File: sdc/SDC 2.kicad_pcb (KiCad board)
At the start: 2 copper layers, 70 x 45 mm, 90 parts, among them J1 Conn_02x10_Odd_Even, K1 G2RL-2A, K2 G2RL-2A, K3 G2RL-2A, K4 G2RL-2A, Q1 2N7002, Q2 2N7002, Q3 2N7002, Q4 2N7002, Q5 2N7002, Q6 2N7002, U1 VOM618AT, U10 AP2204K-ADJ, U2 VOM618AT, U3 TLV2371DBV, U4 TLV2371DBV, U6 VOM618AT, U7 VOM618AT, U8 TLV2371DBV, U9 AP2204K-ADJ

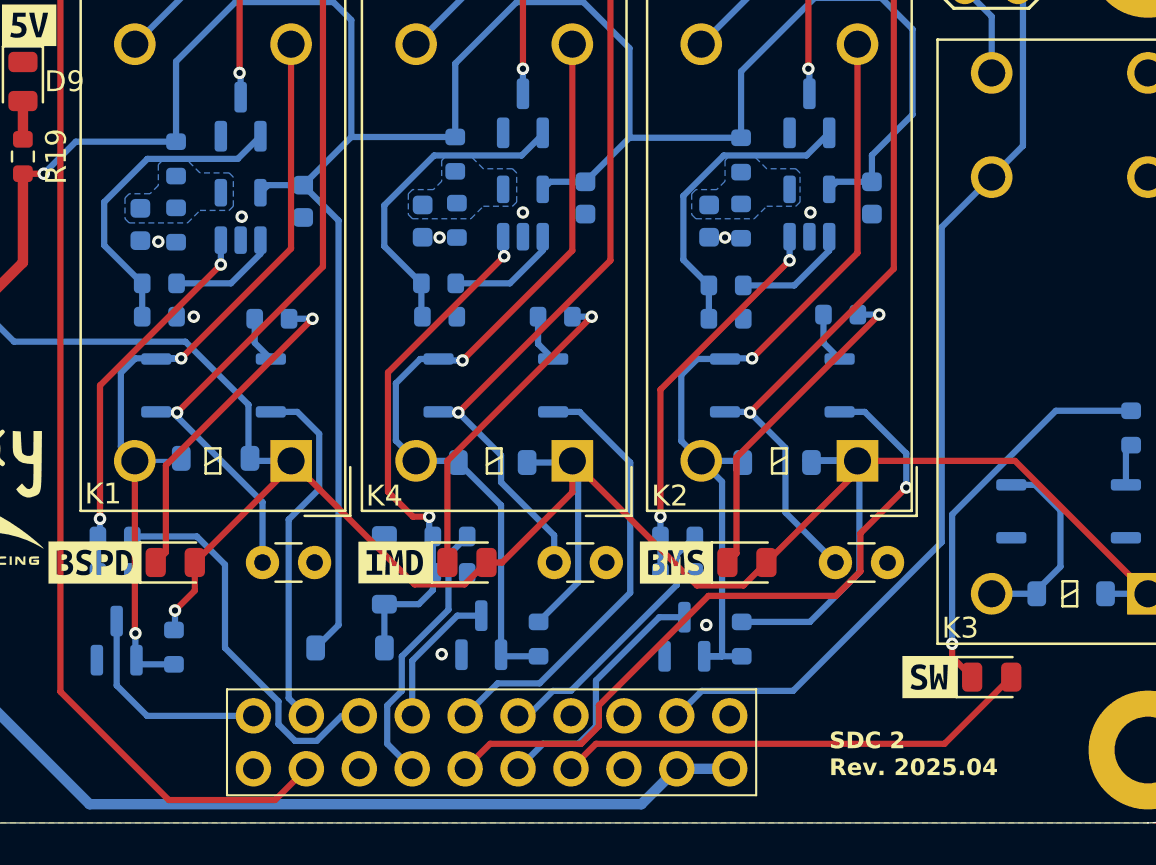
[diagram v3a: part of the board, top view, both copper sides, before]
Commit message: change comparator to AS331KTR-G1
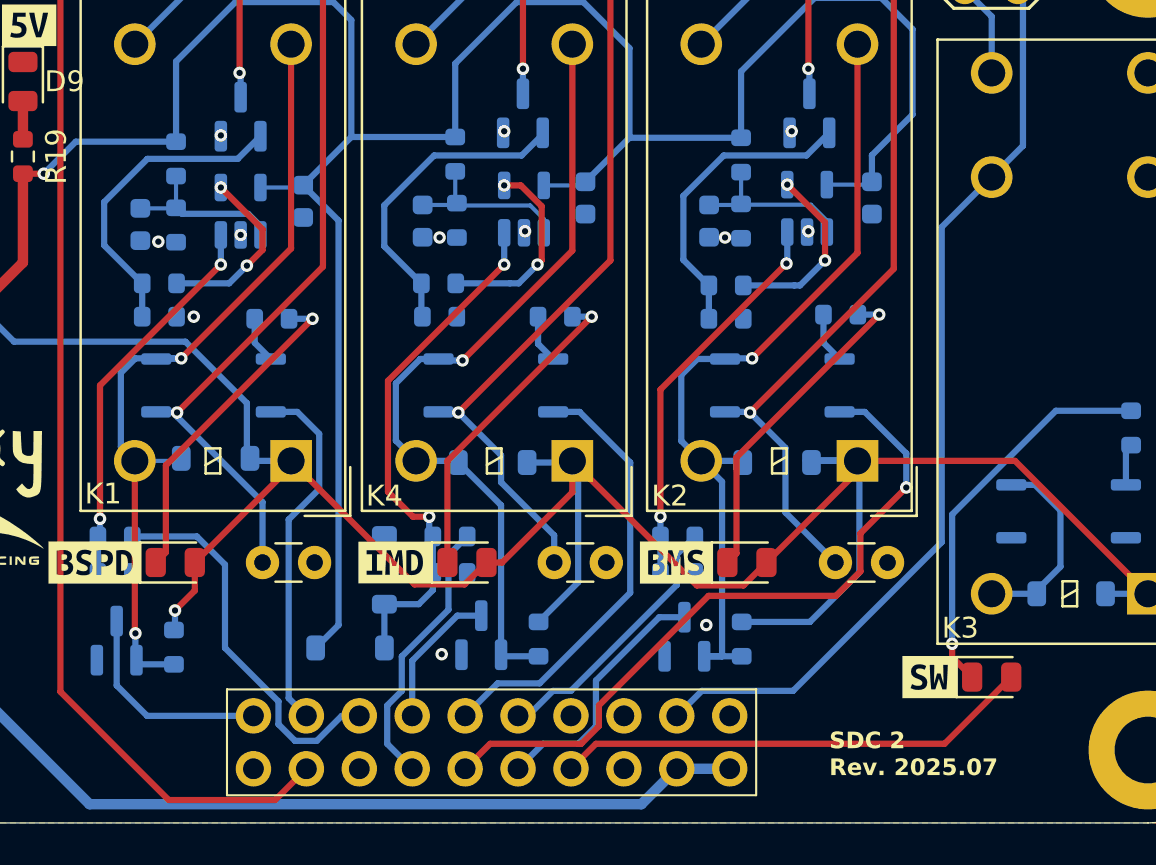
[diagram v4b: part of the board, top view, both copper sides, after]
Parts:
- removed U8: TLV2371DBV, Package_TO_SOT_SMD:SOT-23-5
- added U5: AS331KTR-G1, Package_TO_SOT_SMD:SOT-23-5, B.Cu at (89.5, 63.5)
- U3, U4: value TLV2371DBV -> AS331KTR-G1
- moved U4 0.25 mm to (103.1, 63.5)
- moved U3 0.25 mm to (76.0, 63.6)
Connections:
- U3 pad 1: Net-(R13-Pad1) -> Net-(U3--)
- U3 pad 4: Net-(U3--) -> Net-(R13-Pad1)
- U4 pad 1: Net-(R14-Pad1) -> Net-(U4--)
- U4 pad 4: Net-(U4--) -> Net-(R14-Pad1)
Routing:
- net Net-(U5--): track 0.00 -> 8.39 mm
- net Net-(U4--): track 0.00 -> 8.08 mm
- net Net-(U3--): track 0.04 -> 8.09 mm
- net Net-(R27-Pad1): track 5.49 -> 9.39 mm, vias 0 -> 2
- net Net-(R13-Pad1): track 5.27 -> 8.62 mm, vias 0 -> 2
- net Net-(R14-Pad1): track 5.48 -> 8.81 mm, vias 0 -> 2
- net GND: vias 10 -> 13
- removed copper zone on B.Cu, net Net-(U3--)
- removed copper zone on B.Cu, net Net-(U4--)
- removed copper zone on B.Cu, net Net-(U5--)
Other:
- board text added: "SDC 2 Rev. 2025.07"
- board text removed: "SDC 2 Rev. 2025.04"

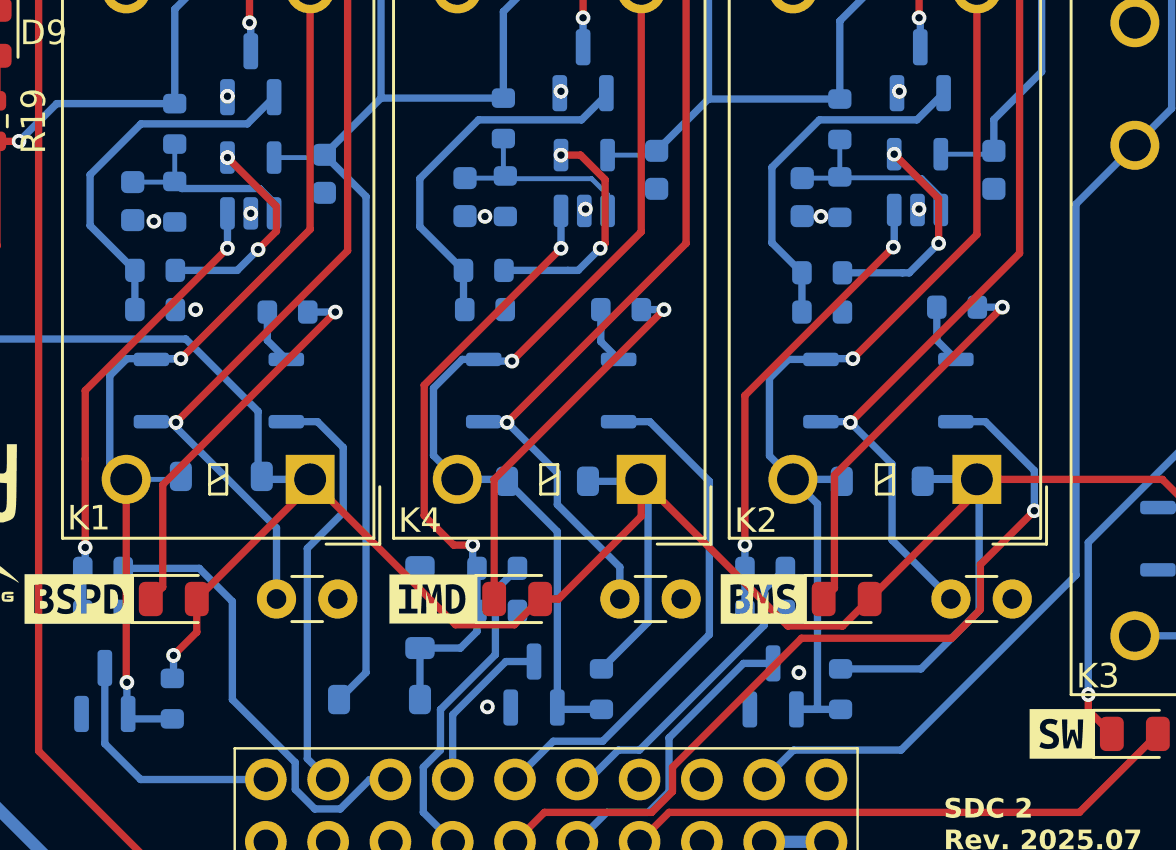
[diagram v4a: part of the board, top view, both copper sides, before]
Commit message: add pull up Resistor
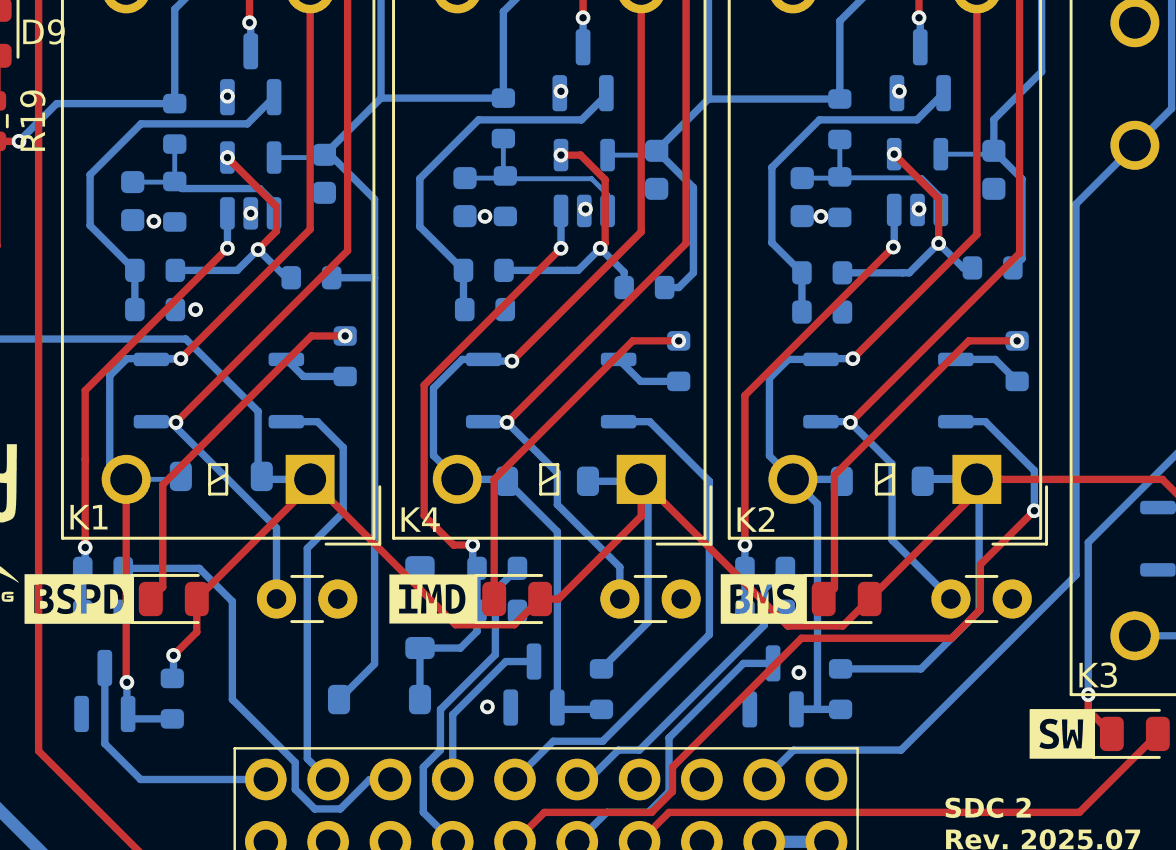
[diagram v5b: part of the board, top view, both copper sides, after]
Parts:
- added R11: 3k, Resistor_SMD:R_0603_1608Metric, B.Cu at (78.4, 67.4)
- added R12: 3k, Resistor_SMD:R_0603_1608Metric, B.Cu at (106.2, 67.0)
- added R26: 3k, Resistor_SMD:R_0603_1608Metric, B.Cu at (92.0, 67.8)
- moved R4 3.29 mm to (107.2, 70.8), turned to -90 degrees
- moved R21 3.15 mm to (93.4, 70.8), turned to -90 degrees
- moved R3 2.96 mm to (79.8, 70.6), turned to -90 degrees
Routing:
- net +5V: track 126.8 -> 141.4 mm
- net Net-(R26-Pad2): track 9.39 -> 11.4 mm
- net Net-(R11-Pad2): track 8.62 -> 10.4 mm
- net Net-(R12-Pad2): track 8.81 -> 10.6 mm
- net Net-(D1-K): track 15.9 -> 14.8 mm
- net Net-(D2-K): track 15.9 -> 14.9 mm
- net Net-(D10-K): track 15.6 -> 14.7 mm
